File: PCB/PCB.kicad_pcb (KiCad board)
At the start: 2 copper layers, 185.4 x 95.2 mm, 20 parts, among them J1 CONN_PWR, J2 BARREL_JACK, J3 CONN_PWR, J4 CONN_02X04, U1 TLC5940NT, U10 ATMEGA328-PU, U2 TLC5940NT, U3 7805

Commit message: WIP
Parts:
- removed J1: CONN_PWR, Connectors:IDC_Header_Straight_8pins
- removed J2: BARREL_JACK, Connectors:BARREL_JACK
- removed J4, J_OUT1: CONN_02X04, Connectors:IDC_Header_Straight_8pins
- removed U10: ATMEGA328-PU, Housings_DIP:DIP-28_W7.62mm
- removed U3: 7805, Power_Integrations:TO-220
- J3: moved to B.Cu
- J_IN1: value CONN_02X04 -> CONN_IF; footprint Connectors:IDC_Header_Straight_8pins -> Connectors:IDC_Header_Straight_10pins; moved to B.Cu
- L1, L2, L3, L4: footprint Displays_7-Segment:7SegmentLED_SBC18-11EGWA -> footprint:KYX-23101BS
- R1, R2: footprint Resistors_THT:R_Axial_DIN0207_L6.3mm_D2.5mm_P7.62mm_Horizontal -> Resistors_THT:R_Axial_DIN0207_L6.3mm_D2.5mm_P10.16mm_Horizontal
- moved J_IN1 99.7 mm to (158.8, 59.1), turned to 90 degrees
- moved J3 75.7 mm to (195.9, 113.7)
- moved L4 49.8 mm to (233.0, 107.0)
- moved L3 44.6 mm to (184.8, 107.0)
- moved R2 44.1 mm to (205.1, 59.7), turned to 90 degrees
- moved L2 41.3 mm to (136.5, 107.0)
- moved L1 40.3 mm to (88.3, 107.0)
- moved REF** 28.6 mm to (262.3, 33.0)
- moved REF** 28.0 mm to (261.6, 113.7)
- moved U2 24.2 mm to (225.4, 71.8)
- moved R1 6.02 mm to (108.6, 61.6), turned to 90 degrees
- moved U1 4.02 mm to (128.9, 71.8)
- moved REF** 2.29 mm to (59.7, 113.7)
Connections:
- J_IN1 pad 6: Net-(J_IN1-Pad6) -> /led-module/SOUT
- J_IN1 pad 7: (no net) -> Net-(J_IN1-Pad7)
- J_IN1 pad 8: (no net) -> Net-(J_IN1-Pad8)
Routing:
- net /led-module/VLED: track 0.00 -> 130.2 mm
- net /led-module/2SEG_A: track 0.00 -> 86.5 mm
- net /led-module/2SEG_B: track 0.00 -> 86.0 mm, vias 0 -> 2
- net /led-module/1SEG_F: track 0.00 -> 75.6 mm, vias 0 -> 2
- net /led-module/2SEG_F: track 0.00 -> 73.3 mm
- net /led-module/1SEG_G: track 0.00 -> 71.8 mm, vias 0 -> 2
- net /led-module/2SEG_G: track 0.00 -> 71.1 mm
- net /led-module/1SEG_C: track 0.00 -> 63.3 mm
- net /led-module/1SEG_E: track 0.00 -> 63.1 mm
- net /led-module/1SEG_D: track 0.00 -> 63.1 mm
- net /led-module/2DP: track 0.00 -> 62.5 mm, vias 0 -> 2
- net /led-module/1DP: track 0.00 -> 60.3 mm, vias 0 -> 2
- net /led-module/2SEG_E: track 0.00 -> 59.8 mm, vias 0 -> 2
- net /led-module/2SEG_D: track 0.00 -> 59.1 mm, vias 0 -> 2
- net /led-module/2SEG_C: track 0.00 -> 57.2 mm, vias 0 -> 2
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- added copper zone on F.Cu, net Earth
- removed copper zone on B.Cu, net Earth
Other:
- board size 185.4 x 95.2 mm -> 215.9 x 95.3 mm
- net class Default: trace_width 0.25 -> 0.2
- net class POWER added: clearance 0.4, trace_width 1, via_dia 1, via_drill 0.8
- net class Signal added: clearance 0.4, trace_width 1, via_dia 1, via_drill 0.8

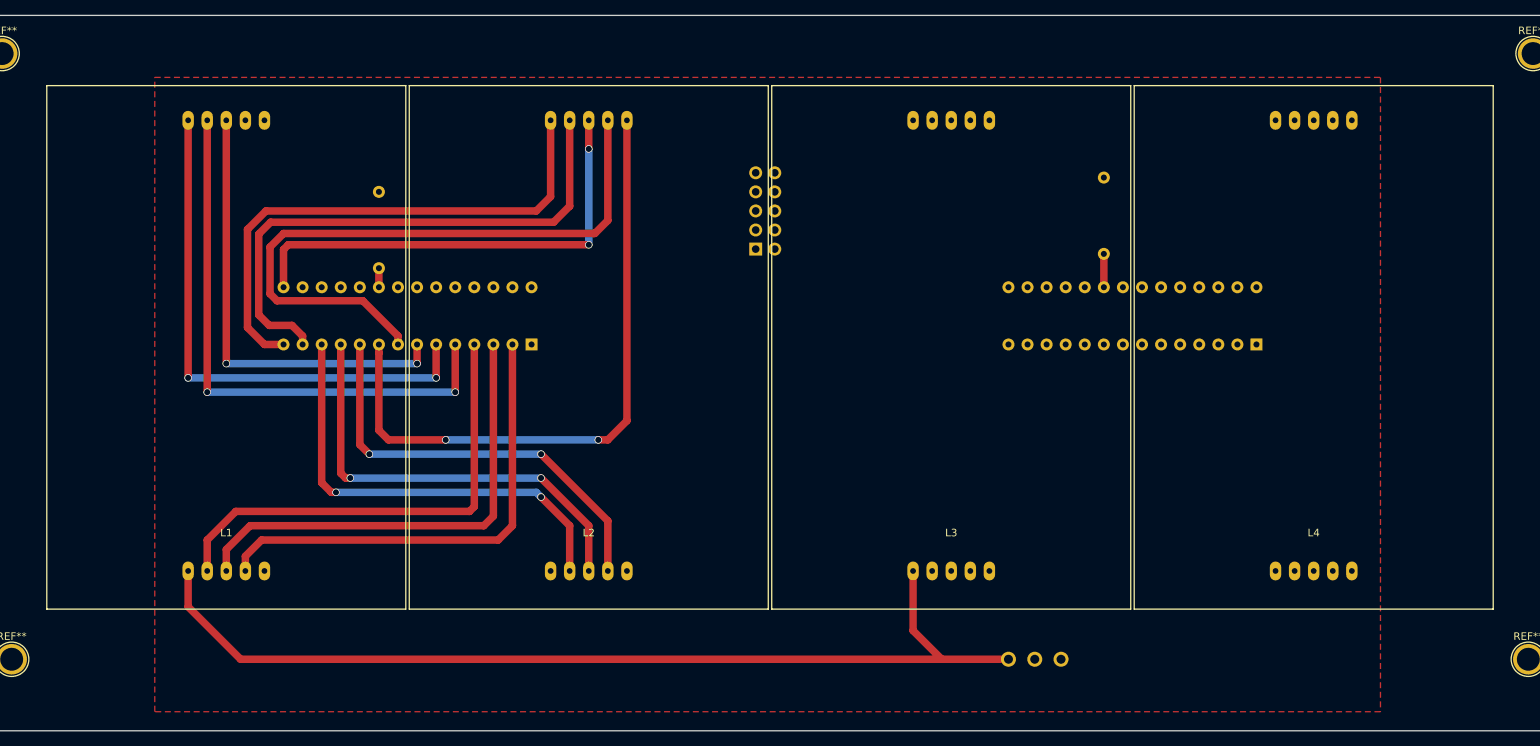
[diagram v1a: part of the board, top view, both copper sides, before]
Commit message: Перегруппировка коннекторов модуля
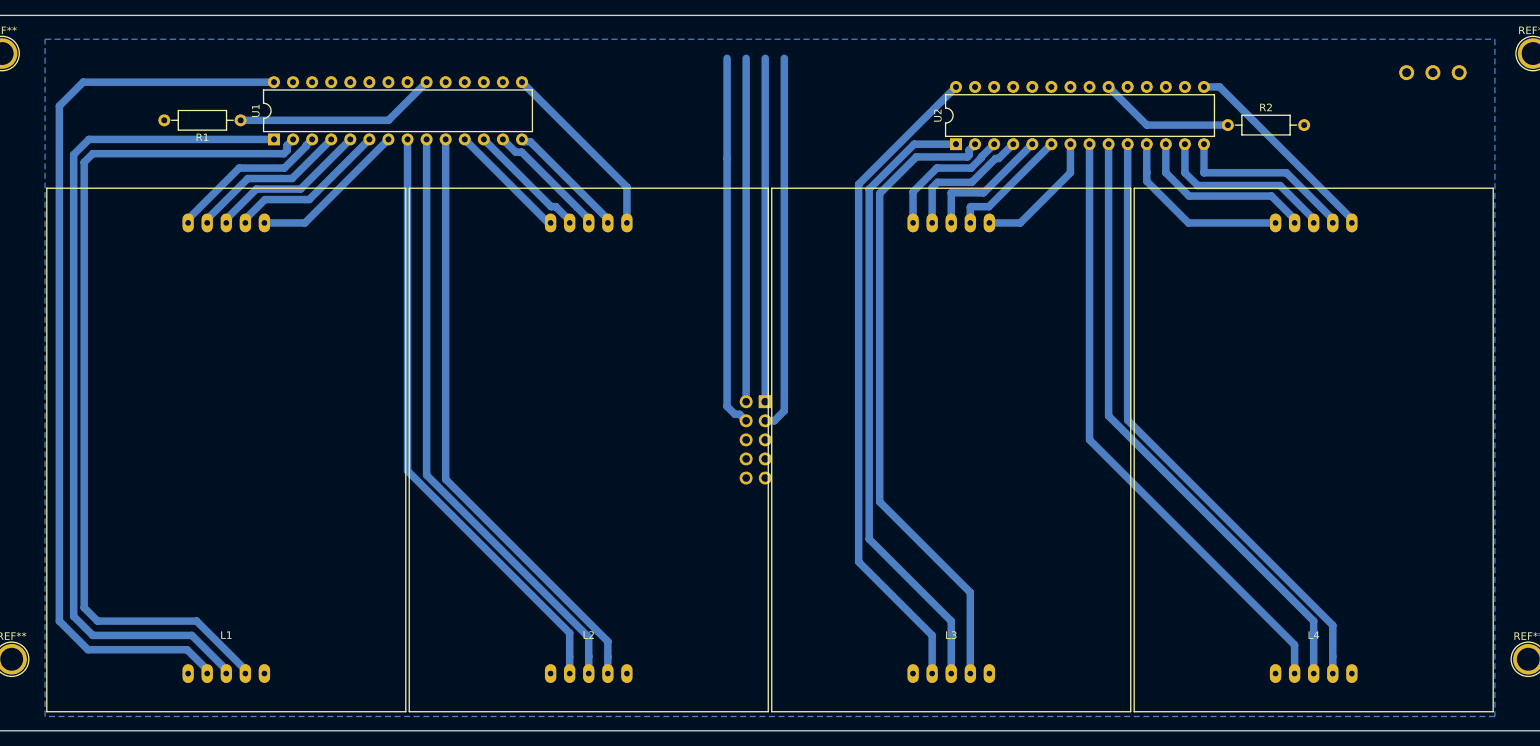
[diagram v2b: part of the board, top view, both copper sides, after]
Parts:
- R1, R2, U1, U2: moved to F.Cu
- moved J3 94.4 mm to (248.9, 35.6)
- moved U2 48.1 mm to (185.4, 45.1)
- moved U1 43.8 mm to (94.6, 44.5)
- moved R1 27.0 mm to (90.2, 41.9), turned to 180 degrees
- moved R2 23.8 mm to (221.6, 42.5), turned to 0 degrees
- moved J_IN1 20.4 mm to (160.0, 79.4), turned to 270 degrees
- moved L1 13.7 mm to (88.3, 120.7)
- moved L2 13.7 mm to (136.5, 120.7)
- moved L3 13.7 mm to (184.8, 120.7)
- moved L4 13.7 mm to (233.0, 120.7)
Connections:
- U1 pad 1: /led-module/1SEG_B -> /led-module/1SEG_D
- U1 pad 11: /led-module/2SEG_D -> /led-module/2SEG_G
- U1 pad 12: /led-module/2SEG_E -> /led-module/2SEG_F
- U1 pad 13: /led-module/2SEG_F -> /led-module/2DP
- U1 pad 14: /led-module/2SEG_G -> /led-module/2SEG_A
- U1 pad 15: /led-module/2DP -> /led-module/2SEG_B
- U1 pad 28: /led-module/1SEG_A -> /led-module/1SEG_E
- U1 pad 3: /led-module/1SEG_D -> /led-module/1SEG_G
- U1 pad 4: /led-module/1SEG_E -> /led-module/1SEG_F
- U1 pad 5: /led-module/1SEG_F -> /led-module/1DP
- U1 pad 6: /led-module/1SEG_G -> /led-module/1SEG_A
- U1 pad 7: /led-module/1DP -> /led-module/1SEG_B
- U1 pad 8: /led-module/2SEG_A -> /led-module/2SEG_E
- U1 pad 9: /led-module/2SEG_B -> /led-module/2SEG_D
- U2 pad 1: /led-module/3SEG_B -> /led-module/3SEG_D
- U2 pad 11: /led-module/4SEG_D -> /led-module/4SEG_G
- U2 pad 12: /led-module/4SEG_E -> /led-module/4SEG_F
- U2 pad 13: /led-module/4SEG_F -> /led-module/4DP
- U2 pad 14: /led-module/4SEG_G -> /led-module/4SEG_A
- U2 pad 15: /led-module/4DP -> /led-module/4SEG_B
- U2 pad 28: /led-module/3SEG_A -> /led-module/3SEG_E
- U2 pad 3: /led-module/3SEG_D -> /led-module/3SEG_G
- U2 pad 4: /led-module/3SEG_E -> /led-module/3SEG_F
- U2 pad 5: /led-module/3SEG_F -> /led-module/3DP
- U2 pad 6: /led-module/3SEG_G -> /led-module/3SEG_A
- U2 pad 7: /led-module/3DP -> /led-module/3SEG_B
- U2 pad 8: /led-module/4SEG_A -> /led-module/4SEG_E
- U2 pad 9: /led-module/4SEG_B -> /led-module/4SEG_D
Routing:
- net /led-module/VLED: track 130.2 -> 0.00 mm
- net /led-module/3SEG_E: track 0.00 -> 87.5 mm
- net /led-module/3SEG_C: track 0.00 -> 84.7 mm
- net /led-module/3SEG_D: track 0.00 -> 83.1 mm
- net /led-module/4SEG_C: track 0.00 -> 81.8 mm
- net /led-module/4SEG_E: track 0.00 -> 81.8 mm
- net /led-module/4SEG_D: track 0.00 -> 81.8 mm
- net /led-module/2SEG_A: track 86.5 -> 16.3 mm
- net /led-module/2SEG_B: track 86.0 -> 24.5 mm, vias 2 -> 0
- net /led-module/1SEG_E: track 63.1 -> 121.3 mm
- net /led-module/2SEG_F: track 73.3 -> 16.2 mm
- net /led-module/2SEG_G: track 71.1 -> 16.0 mm
- net /led-module/1SEG_F: track 75.6 -> 21.4 mm, vias 2 -> 0
- net /led-module/1SEG_C: track 63.3 -> 114.2 mm
- net /led-module/1SEG_G: track 71.8 -> 21.5 mm, vias 2 -> 0
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- added copper zone on B.Cu, net Earth
- removed copper zone on F.Cu, net Earth

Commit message: tracing
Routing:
- net /led-module/SIN: track 0.00 -> 124.1 mm, vias 0 -> 2
- net /led-module/SOUT: track 0.00 -> 108.9 mm, vias 0 -> 1
- net /led-module/SCLK: track 45.7 -> 145.0 mm, vias 0 -> 1
- net /led-module/BLANK: track 50.0 -> 145.1 mm, vias 0 -> 2
- net Net-(U1-Pad17): track 0.00 -> 70.4 mm, vias 0 -> 3
- net /led-module/XLAT: track 45.7 -> 94.1 mm, vias 0 -> 2
- net /led-module/GSCLK: track 49.7 -> 87.8 mm
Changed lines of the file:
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@@
   (general
     (links 63)
-    (no_connects 22)
-    (area 36.837858 27.889999 269.290001 135.415001)
+    (no_connects 21)
+    (area 53.289999 27.889999 269.290001 123.240001)
     (thickness 1.6)
     (drawings 13)
-    (tracks 158)
+    (tracks 214)
     (zones 0)
     (modules 14)
@@
   (gr_line (start 269.24 120.65) (end 269.24 30.48) (angle 90) (layer Edge.Cuts) (width 0.1))
   (gr_line (start 55.88 123.19) (end 266.7 123.19) (angle 90) (layer Edge.Cuts) (width 0.1))
+  (segment (start 193.04 32.25499) (end 193.04 37.465) (width 1) (layer F.Cu) (net 4))
+  (via (at 193.04 32.25499) (size 1) (drill 0.8) (layers F.Cu B.Cu) (net 4))
+  (segment (start 160.02 32.385) (end 161.850087 32.385) (width 1) (layer B.Cu) (net 4))
+  (segment (start 161.850087 32.385) (end 161.980097 32.25499) (width 1) (layer B.Cu) (net 4))
+  (segment (start 161.980097 32.25499) (end 193.04 32.25499) (width 1) (layer B.Cu) (net 4))
+  (segment (start 159.88999 32.25499) (end 160.02 32.385) (width 1) (layer B.Cu) (net 4))
+  (segment (start 160.02 32.385) (end 160.02 33.655) (width 1) (layer B.Cu) (net 4))
+  (segment (start 102.235 36.83) (end 106.81001 32.25499) (width 1) (layer B.Cu) (net 4))
+  (segment (start 106.81001 32.25499) (end 159.88999 32.25499) (width 1) (layer B.Cu) (net 4))
   (segment (start 160.02 79.375) (end 160.02 33.655) (width 1) (layer B.Cu) (net 4))
-  (segment (start 157.48 79.375) (end 157.48 33.655) (width 1) (layer B.Cu) (net 5))
-  (segment (start 162.56 80.596314) (end 162.56 33.655) (width 1) (layer B.Cu) (net 6))
+  (segment (start 157.48 79.375) (end 157.48 40.64) (width 1) (layer B.Cu) (net 5))
+  (segment (start 157.48 40.64) (end 157.35 40.51) (width 1) (layer B.Cu) (net 5))
+  (via (at 157.35 40.51) (size 1) (drill 0.8) (layers F.Cu B.Cu) (net 5))
+  (segment (start 106.68 40.51) (end 157.35 40.51) (width 1) (layer F.Cu) (net 5))
+  (segment (start 104.775 36.83) (end 104.775 38.605) (width 1) (layer B.Cu) (net 5))
+  (via (at 106.68 40.51) (size 1) (drill 0.8) (layers F.Cu B.Cu) (net 5))
+  (segment (start 104.775 38.605) (end 106.68 40.51) (width 1) (layer B.Cu) (net 5))
+  (segment (start 162.56 38.735) (end 162.56 33.655) (width 1) (layer B.Cu) (net 6))
+  (segment (start 162.56 33.655) (end 196.85 33.655) (width 1) (layer B.Cu) (net 6))
+  (segment (start 196.85 33.655) (end 198.12 34.925) (width 1) (layer B.Cu) (net 6))
+  (segment (start 198.12 34.925) (end 198.12 37.465) (width 1) (layer B.Cu) (net 6))
+  (segment (start 162.56 80.596314) (end 162.56 38.735) (width 1) (layer B.Cu) (net 6))
+  (segment (start 108.585 38.735) (end 162.56 38.735) (width 1) (layer F.Cu) (net 6))
+  (via (at 162.56 38.735) (size 1) (drill 0.8) (layers F.Cu B.Cu) (net 6))
+  (segment (start 107.315 36.83) (end 107.315 37.465) (width 1) (layer B.Cu) (net 6))
+  (segment (start 107.315 37.465) (end 108.585 38.735) (width 1) (layer B.Cu) (net 6))
+  (via (at 108.585 38.735) (size 1) (drill 0.8) (layers F.Cu B.Cu) (net 6))
   (segment (start 160.02 81.915) (end 161.241314 81.915) (width 1) (layer B.Cu) (net 6))
   (segment (start 161.241314 81.915) (end 162.56 80.596314) (width 1) (layer B.Cu) (net 6))
-  (segment (start 154.94 46.99) (end 154.94 33.655) (width 1) (layer B.Cu) (net 7))
-  (segment (start 154.94 80.01) (end 154.94 46.99) (width 1) (layer B.Cu) (net 7))
-  (segment (start 155.981401 81.051401) (end 154.94 80.01) (width 1) (layer B.Cu) (net 7))
   (segment (start 157.48 81.915) (end 156.616401 81.051401) (width 1) (layer B.Cu) (net 7))
   (segment (start 156.616401 81.051401) (end 155.981401 81.051401) (width 1) (layer B.Cu) (net 7))
+  (segment (start 155.981401 81.051401) (end 154.94 80.01) (width 1) (layer B.Cu) (net 7))
+  (segment (start 154.94 80.01) (end 154.94 33.655) (width 1) (layer B.Cu) (net 7))
+  (segment (start 154.94 33.655) (end 120.015 33.655) (width 1) (layer B.Cu) (net 7))
+  (segment (start 120.015 33.655) (end 120.015 36.83) (width 1) (layer B.Cu) (net 7))
+  (segment (start 163.83 93.98) (end 163.83 85.725) (width 1) (layer B.Cu) (net 8))
+  (segment (start 163.83 85.725) (end 162.56 84.455) (width 1) (layer B.Cu) (net 8))
+  (segment (start 162.56 84.455) (end 160.02 84.455) (width 1) (layer B.Cu) (net 8))
+  (segment (start 91.44 34.925) (end 92.914999 36.399999) (width 1) (layer F.Cu) (net 8))
+  (segment (start 92.914999 36.399999) (end 92.914999 45.970001) (width 1) (layer F.Cu) (net 8))
+  (segment (start 92.914999 45.970001) (end 140.924998 93.98) (width 1) (layer F.Cu) (net 8))
+  (segment (start 140.924998 93.98) (end 163.83 93.98) (width 1) (layer F.Cu) (net 8))
+  (via (at 163.83 93.98) (size 1) (drill 0.8) (layers F.Cu B.Cu) (net 8))
+  (segment (start 99.695 36.83) (end 97.79 34.925) (width 1) (layer B.Cu) (net 8))
+  (via (at 91.44 34.925) (size 1) (drill 0.8) (layers F.Cu B.Cu) (net 8))
+  (segment (start 97.79 34.925) (end 91.44 34.925) (width 1) (layer B.Cu) (net 8))
+  (segment (start 210.82 42.545) (end 213.36 40.005) (width 1) (layer F.Cu) (net 9))
+  (segment (start 213.36 40.005) (end 213.36 37.465) (width 1) (layer F.Cu) (net 9))
+  (segment (start 153.035 42.545) (end 210.82 42.545) (width 1) (layer F.Cu) (net 9))
+  (segment (start 152.4 43.18) (end 153.035 42.545) (width 1) (layer F.Cu) (net 9))
+  (segment (start 152.4 44.45) (end 152.4 43.18) (width 1) (layer F.Cu) (net 9))
+  (segment (start 157.48 84.455) (end 156.258686 84.455) (width 1) (layer B.Cu) (net 9))
+  (segment (start 156.258686 84.455) (end 152.4 80.596314) (width 1) (layer B.Cu) (net 9))
+  (segment (start 152.4 80.596314) (end 152.4 44.45) (width 1) (layer B.Cu) (net 9))
+  (via (at 152.4 44.45) (size 1) (drill 0.8) (layers F.Cu B.Cu) (net 9))
   (segment (start 69.85 112.395) (end 83.05 112.395) (width 1) (layer B.Cu) (net 14))
   (segment (start 83.05 112.395) (end 85.725 115.07) (width 1) (layer B.Cu) (net 14))
@@
   (segment (start 221.615 42.545) (end 210.82 42.545) (width 1) (layer B.Cu) (net 47))
   (segment (start 210.82 42.545) (end 205.74 37.465) (width 1) (layer B.Cu) (net 47))
+  (segment (start 190.5 36.195) (end 190.5 37.465) (width 1) (layer B.Cu) (net 49))
+  (segment (start 189.36 35.055) (end 190.5 36.195) (width 1) (layer B.Cu) (net 49))
+  (segment (start 188.09 35.055) (end 189.36 35.055) (width 1) (layer B.Cu) (net 49))
+  (via (at 188.09 35.055) (size 1) (drill 0.8) (layers F.Cu B.Cu) (net 49))
+  (segment (start 164.97 35.055) (end 188.09 35.055) (width 1) (layer F.Cu) (net 49))
+  (via (at 164.97 35.055) (size 1) (drill 0.8) (layers F.Cu B.Cu) (net 49))
+  (segment (start 151.765 35.055) (end 164.97 35.055) (width 1) (layer F.Cu) (net 49))
+  (segment (start 122.555 36.83) (end 124.33 35.055) (width 1) (layer B.Cu) (net 49))
+  (segment (start 124.33 35.055) (end 124.353998 35.055) (width 1) (layer B.Cu) (net 49))
+  (segment (start 124.353998 35.055) (end 151.765 35.055) (width 1) (layer B.Cu) (net 49))
+  (via (at 151.765 35.055) (size 1) (drill 0.8) (layers F.Cu B.Cu) (net 49))
   (zone (net 1) (net_name Earth) (layer B.Cu) (hatch edge 0.508)
     (connect_pads (clearance 0.508))

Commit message: layoyt changed
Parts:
- removed L3, L4: KYX-23101BS, footprint:KYX-23101BS
- removed R2: 2k, Resistors_THT:R_Axial_DIN0207_L6.3mm_D2.5mm_P10.16mm_Horizontal
- removed REF** (x4): 1pin, Connectors:1pin
- removed U2: TLC5940NT, Housings_DIP:DIP-28_W7.62mm
- J3: moved to F.Cu
- R1: moved to B.Cu
- moved J3 190.9 mm to (88.1, 138.3)
- moved J_IN1 56.9 mm to (109.1, 53.9), turned to 0 degrees
- moved R1 53.1 mm to (51.8, 78.6), turned to 90 degrees
- moved U1 42.6 mm to (55.3, 60.9)
- moved L1 26.2 mm to (65.4, 133.3)
- moved L2 26.2 mm to (113.7, 133.3)
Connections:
- U1 pad 17: Net-(U1-Pad17) -> /led-module/SOUT
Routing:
- net /led-module/BLANK: track 145.1 -> 0.00 mm, vias 2 -> 0
- net /led-module/SCLK: track 145.0 -> 0.00 mm, vias 1 -> 0
- net /led-module/SIN: track 124.1 -> 0.00 mm, vias 2 -> 0
- net /led-module/SOUT: track 108.9 -> 0.00 mm, vias 1 -> 0
- net /led-module/XLAT: track 94.1 -> 0.00 mm, vias 2 -> 0
- net /led-module/GSCLK: track 87.8 -> 0.00 mm
- net /led-module/3SEG_E: track 87.5 -> 0.00 mm
- net /led-module/3SEG_C: track 84.7 -> 0.00 mm
- net /led-module/3SEG_D: track 83.1 -> 0.00 mm
- net /led-module/4SEG_C: track 81.8 -> 0.00 mm
- net /led-module/4SEG_E: track 81.8 -> 0.00 mm
- net /led-module/4SEG_D: track 81.8 -> 0.00 mm
- net Net-(U1-Pad17): track 70.4 -> 0.00 mm, vias 3 -> 0
- net /led-module/1SEG_C: track 114.2 -> 71.6 mm
- net /led-module/1SEG_D: track 112.7 -> 71.7 mm
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- removed copper zone on B.Cu, net Earth
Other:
- board outline removed
- net class Default: clearance 0.2 -> 1; trace_width 0.2 -> 0.6; via_drill 0.4 -> 0.3
- net class POWER removed
- net class Signal removed
- rule trace_clearance: 0.2 -> 1
- board text removed: "7x3 LED Module rev.1"

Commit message: WIP
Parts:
- added J2: BARREL_JACK, Connectors:BARREL_JACK, F.Cu at (0.00, 0.00)
- added JPWR1, JPWR2, JPWR3: CONN_PWR, Connectors_WAGO:WAGO_734_3pin_Straight, F.Cu at (0.00, 0.00)
- added J_M1, J_M2, J_M3: CONN_IF, Connectors:IDC_Header_Straight_10pins, F.Cu at (0.00, 0.00)
- added U10: ATMEGA328-PU, Housings_DIP:DIP-28_W7.62mm, F.Cu at (0.00, 0.00)
- added U3: 7805, Power_Integrations:TO-220, F.Cu at (0.00, 0.00)
- J3: moved to B.Cu
- moved J_IN1 58.1 mm to (67.2, 94.1)
- moved J3 44.8 mm to (98.6, 94.8), turned to 180 degrees
- moved R1 8.05 mm to (45.6, 73.5), turned to 270 degrees
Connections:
- J_IN1 pad 2: /led-module/XLAT -> /led-module/SIN
- J_IN1 pad 3: /led-module/BLANK -> /led-module/XLAT
- J_IN1 pad 4: /led-module/GSCLK -> Net-(J_IN1-Pad4)
- J_IN1 pad 5: /led-module/SIN -> /led-module/BLANK
- J_IN1 pad 6: /led-module/SOUT -> Net-(J_IN1-Pad6)
- J_IN1 pad 7: Net-(J_IN1-Pad7) -> /led-module/GSCLK
- J_IN1 pad 9: Net-(J_IN1-Pad9) -> /led-module/SOUT
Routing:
- net /led-module/VLED: track 0.00 -> 107.5 mm, vias 0 -> 1
- net /led-module/BLANK: track 0.00 -> 69.3 mm
- net /led-module/SIN: track 0.00 -> 59.7 mm
- net /led-module/XLAT: track 0.00 -> 59.2 mm
- net /led-module/SCLK: track 0.00 -> 58.5 mm
- net /led-module/GSCLK: track 0.00 -> 57.4 mm
- net Net-(R1-Pad1): track 56.7 -> 0.00 mm
- net /led-module/SOUT: track 0.00 -> 55.5 mm
- net Earth: track 23.3 -> 26.1 mm
- net /led-module/2SEG_B: track 40.4 -> 37.8 mm

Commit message: layput complete
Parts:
- removed J2: BARREL_JACK, Connectors:BARREL_JACK
- removed JPWR1, JPWR2, JPWR3: CONN_PWR, Connectors_WAGO:WAGO_734_3pin_Straight
- removed J_M1, J_M2, J_M3: CONN_IF, Connectors:IDC_Header_Straight_10pins
- removed U10: ATMEGA328-PU, Housings_DIP:DIP-28_W7.62mm
- removed U3: 7805, Power_Integrations:TO-220
- U1: moved to B.Cu
- moved R1 45.0 mm to (85.8, 93.8), turned to 0 degrees
- moved J3 43.8 mm to (54.9, 91.4), turned to 90 degrees
- moved U1 24.9 mm to (73.2, 78.2), turned to 270 degrees
- moved J_IN1 23.8 mm to (76.6, 115.9)
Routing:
- net /led-module/VCC: track 0.00 -> 40.6 mm
- net /led-module/BLANK: track 69.3 -> 32.1 mm
- net Earth: track 26.1 -> 58.8 mm
- net /led-module/1SEG_E: track 80.6 -> 50.3 mm, vias 0 -> 1
- net /led-module/XLAT: track 59.2 -> 31.9 mm
- net /led-module/SCLK: track 58.5 -> 31.9 mm
- net /led-module/SIN: track 59.7 -> 35.9 mm
- net /led-module/1SEG_D: track 71.7 -> 53.3 mm
- net /led-module/1SEG_C: track 71.6 -> 53.3 mm
- net /led-module/GSCLK: track 57.4 -> 40.3 mm
- net /led-module/2SEG_F: track 32.7 -> 15.9 mm
- net /led-module/2SEG_A: track 32.1 -> 15.2 mm
- net /led-module/2DP: track 32.7 -> 15.9 mm
- net /led-module/2SEG_G: track 31.7 -> 14.9 mm
- net /led-module/1DP: track 7.39 -> 23.8 mm
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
